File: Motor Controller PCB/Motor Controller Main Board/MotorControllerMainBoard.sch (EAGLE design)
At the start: 83 parts, among them T1 TEENSY_3.1_ALL_PINS

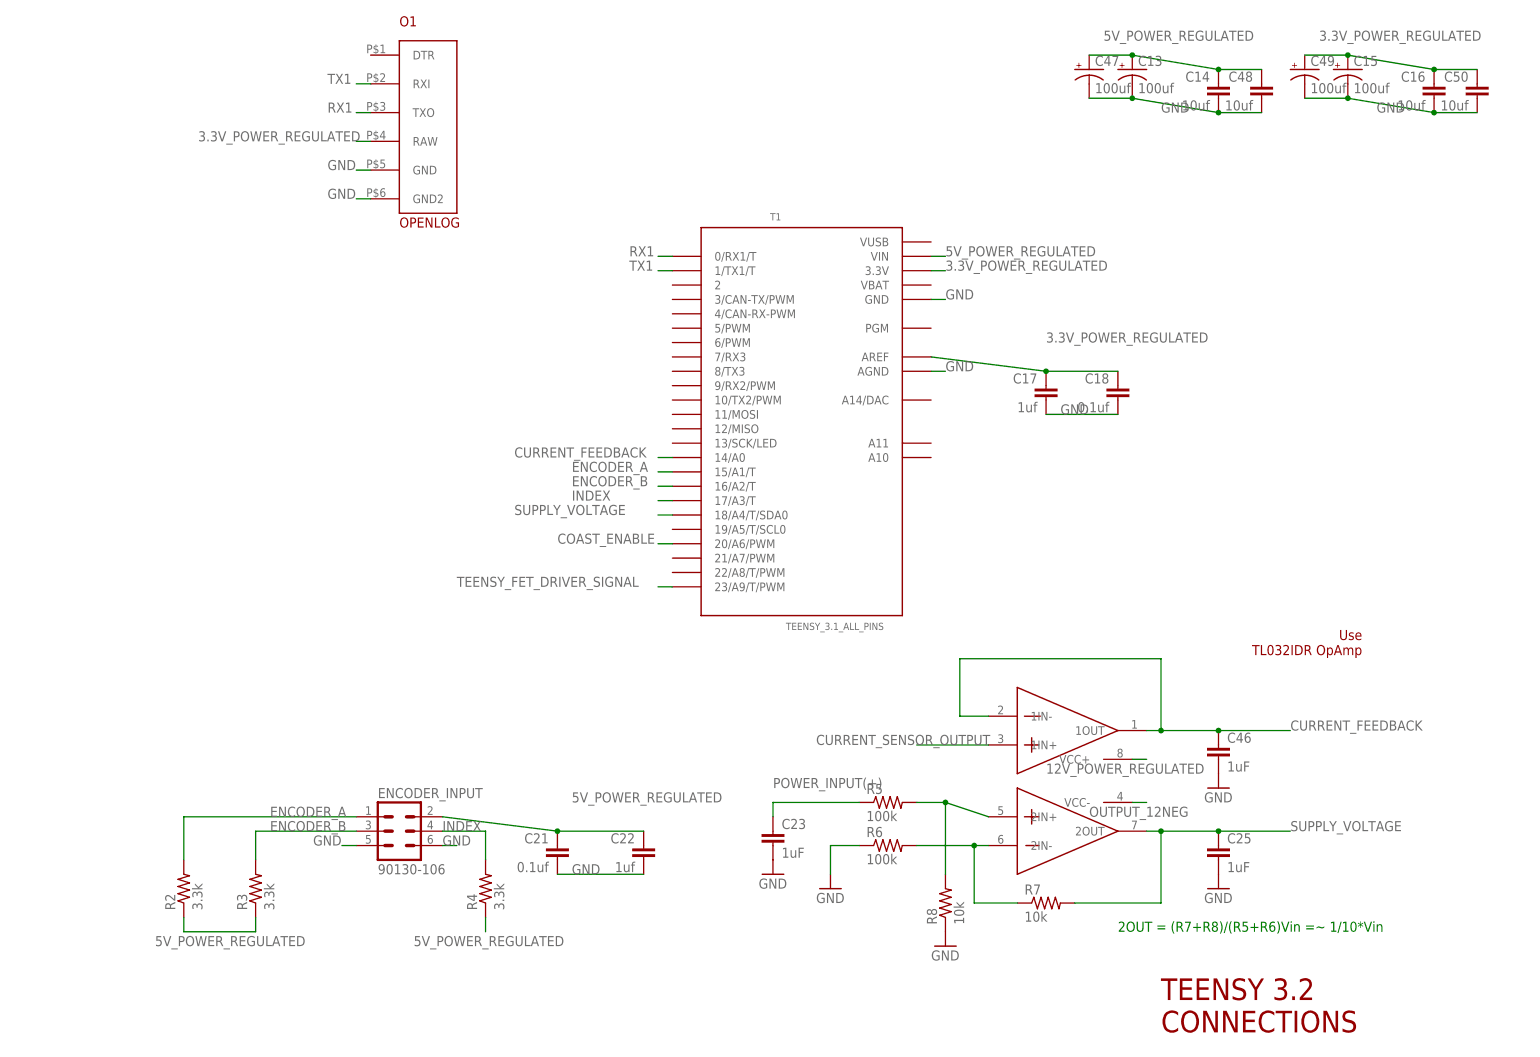
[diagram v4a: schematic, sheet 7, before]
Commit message: Routed majority of the power components
-Only thing left is stuff connected to teensy and other things i missed
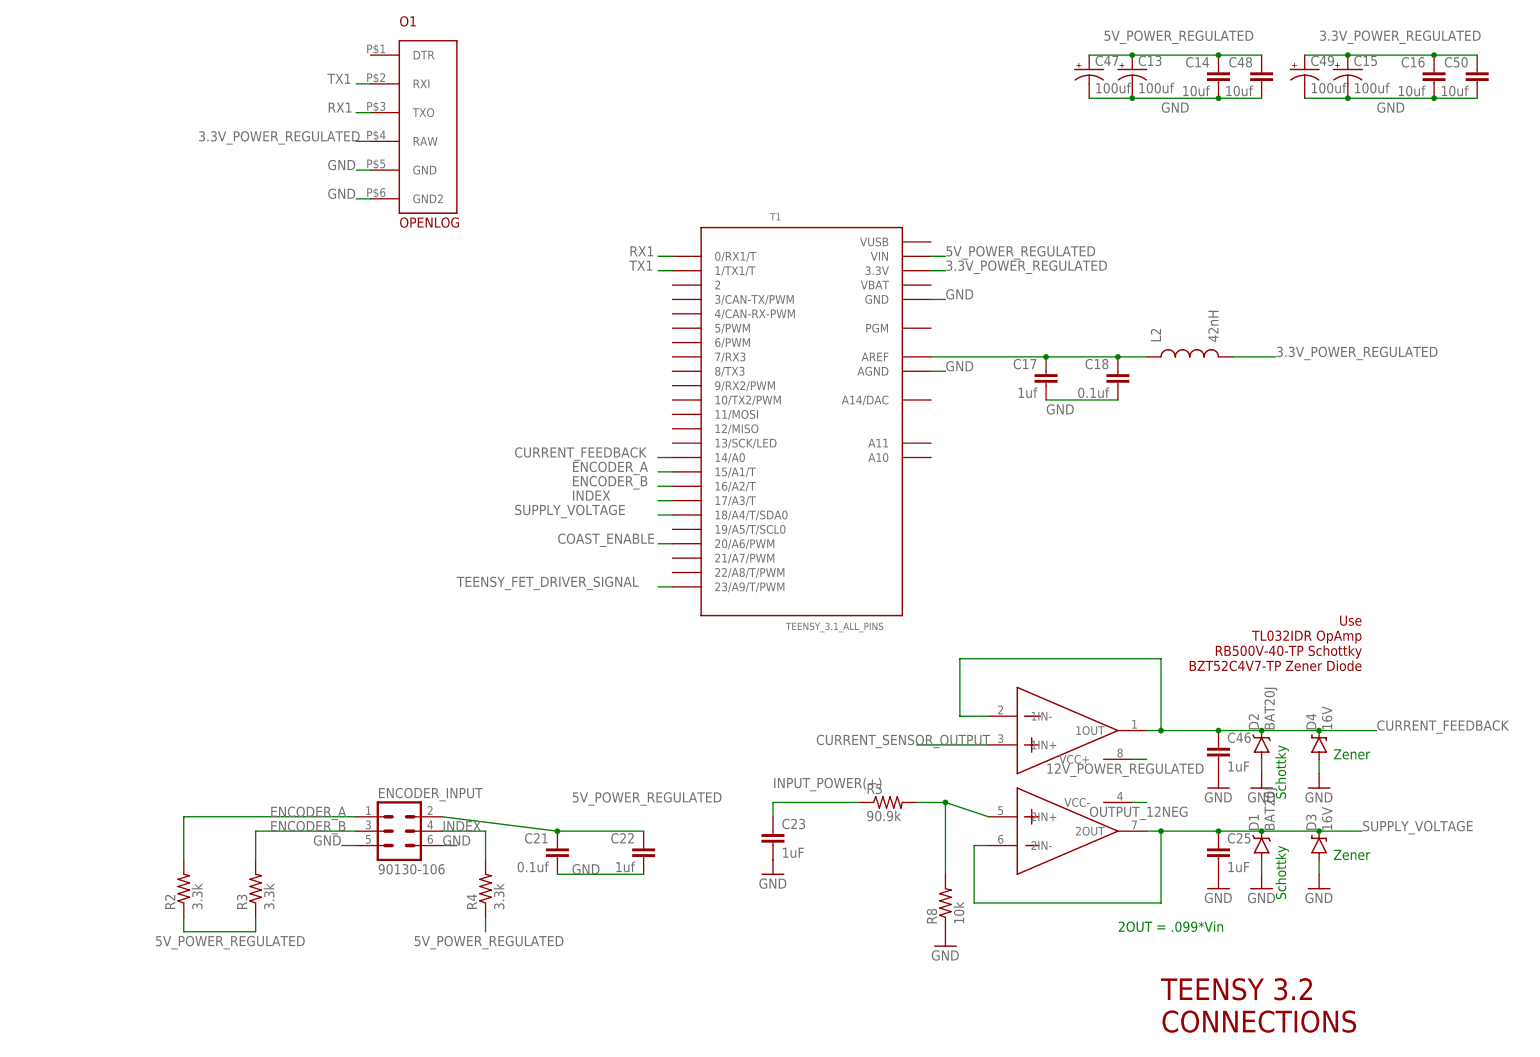
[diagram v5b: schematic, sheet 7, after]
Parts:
- removed R6: 100k, rcl:R-US_R0805
- removed R7: 10k, rcl:R-US_R0805
- added D1, D2: BAT20J, SparkFun-DiscreteSemi:DIODE-SCHOTTKY-BAT20J
- added D3, D4: 16V, SparkFun-DiscreteSemi:DIODE-ZENER16V
- added L2: 42nH, SparkFun (2015_10_14 22_27_04 UTC):INDUCTOR0805
- C55, C56, C57, C59, C60: value (none) -> 10uF
- R5: value 100k -> 90.9k
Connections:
- new net N$13: R9.11, SV2.2
- net 3.3V_POWER_REGULATED: now also L2.2; no longer C17.1, C18.1, T1.AREF
- net CURRENT_FEEDBACK: now also D2.C, D4.C
- net FET_DRIVER_SIGNAL: no longer R9.11, SV2.2
- net GND: now also D1.A, D2.A, D3.A, D4.A; no longer R6.1
- net INPUT_POWER(+): now also C23.1, R5.1
- net MOTOR_OUTPUT_(+): now also U$13.VIN, U$6.VIN
- net N$9: now also C17.1, C18.1, L2.1, T1.AREF; no longer AD8512ARZ.2IN-, R6.2, R7.1
- net POWER_INPUT(+): no longer C23.1, R5.1, U$13.VIN, U$6.VIN
- net SUPPLY_VOLTAGE: now also AD8512ARZ.2IN-, D1.C, D3.C; no longer R7.2
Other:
- note added: "2OUT = .099*Vin"
- note added: "Schottky"
- note added: "Use TL032IDR OpAmp RB500V-40-TP Schottky BZT52C4V7-TP Zener Diode"
- note added: "Zener"
- note removed: "2OUT = (R7+R8)/(R5+R6)Vin =~ 1/10*Vin"
- note removed: "Use TL032IDR OpAmp"
- moved on the sheet: C14, C16, C17, C18, C48, C50

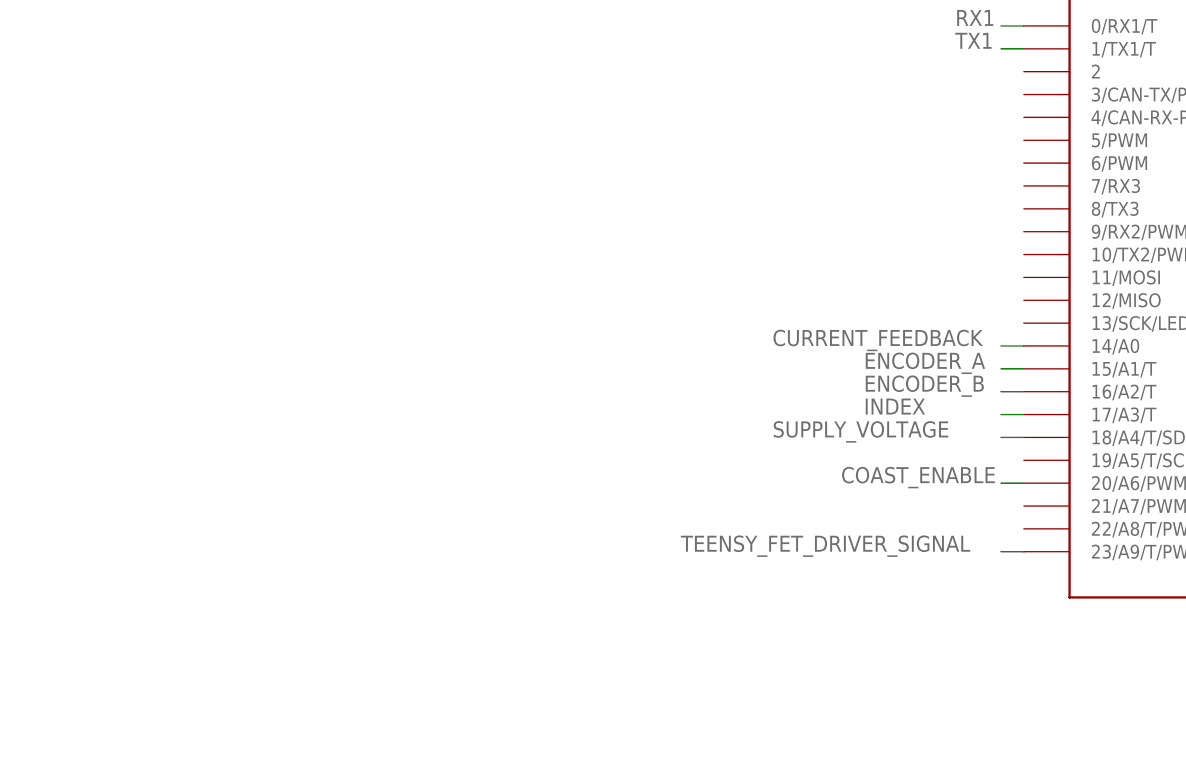
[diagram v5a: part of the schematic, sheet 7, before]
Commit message: Added Header, Worked on Digital Connections
Added 2x5 header for IO, added 1x3 header for Hall sensor. Worked on
some digital connections, still a work in progress.
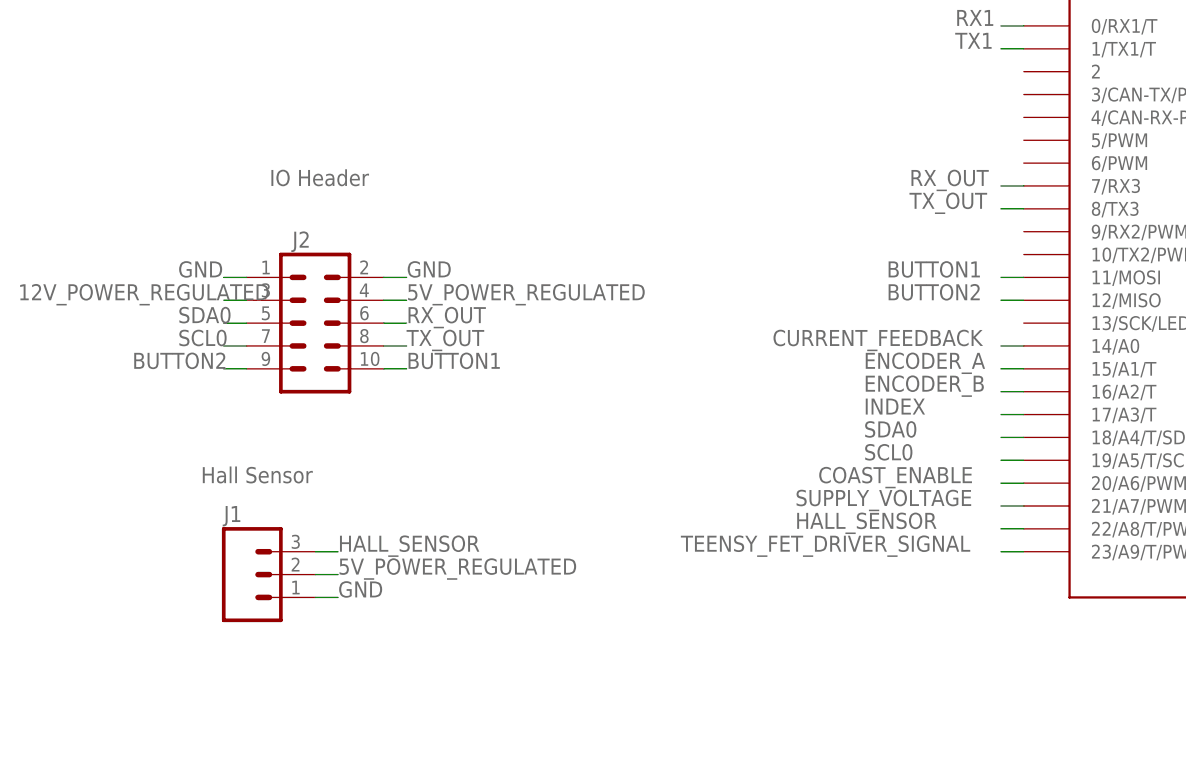
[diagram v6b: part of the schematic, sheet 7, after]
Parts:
- added J1: (no value), SparkFun-Connectors:M03PTH
- added J2: (no value), SparkFun-Connectors:M05X2NO_SILK
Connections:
- new net BUTTON1: J2.10, T1.11/MOSI
- new net BUTTON2: J2.9, T1.12/MISO
- new net HALL_SENSOR: J1.3, T1.22/A8/T/PWM
- new net RX_OUT: J2.6, T1.7/RX3
- new net SCL0: J2.7, T1.19/A5/T/SCL0
- new net SDA0: J2.5, T1.18/A4/T/SDA0
- new net TX_OUT: J2.8, T1.8/TX3
- net 12V_POWER_REGULATED: now also J2.3
- net 5V_POWER_REGULATED: now also J1.2, J2.4
- net GND: now also J1.1, J2.1, J2.2
- net SUPPLY_VOLTAGE: now also T1.21/A7/PWM; no longer T1.18/A4/T/SDA0
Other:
- note added: "Hall Sensor"
- note added: "IO Header"
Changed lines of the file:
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@@
 <part name="GND33" library="E-P-008-R1.2" deviceset="GND" device=""/>
 <part name="L2" library="SparkFun (2015_10_14 22_27_04 UTC)" deviceset="INDUCTOR" device="0805" value="42nH"/>
+<part name="J2" library="SparkFun-Connectors" deviceset="M05X2" device="NO_SILK"/>
+<part name="J1" library="SparkFun-Connectors" deviceset="M03" device="PTH"/>
 </parts>
 <sheets>
@@
 <text x="223.52" y="58.42" size="1.778" layer="91" rot="R270">Schottky</text>
 <text x="223.52" y="76.2" size="1.778" layer="91" rot="R270">Schottky</text>
+<text x="33.02" y="144.78" size="1.778" layer="95">IO Header</text>
+<text x="25.4" y="111.76" size="1.778" layer="95">Hall Sensor</text>
 </plain>
 <instances>
@@
 <instance part="GND33" gate="1" x="231.14" y="50.8"/>
 <instance part="L2" gate="G$1" x="208.28" y="144.78" rot="R90"/>
+<instance part="J2" gate="G$1" x="38.1" y="129.54"/>
+<instance part="J1" gate="J$1" x="30.48" y="101.6"/>
 </instances>
 <busses>
@@
 <wire x1="231.14" y1="55.88" x2="231.14" y2="53.34" width="0.1524" layer="91"/>
 </segment>
+<segment>
+<pinref part="J2" gate="G$1" pin="1"/>
+<wire x1="30.48" y1="134.62" x2="27.94" y2="134.62" width="0.1524" layer="91"/>
+<label x="22.86" y="134.62" size="1.778" layer="95"/>
+</segment>
+<segment>
+<pinref part="J2" gate="G$1" pin="2"/>
+<wire x1="45.72" y1="134.62" x2="48.26" y2="134.62" width="0.1524" layer="91"/>
+<label x="48.26" y="134.62" size="1.778" layer="95"/>
+</segment>
+<segment>
+<pinref part="J1" gate="J$1" pin="1"/>
+<wire x1="38.1" y1="99.06" x2="40.64" y2="99.06" width="0.1524" layer="91"/>
+<label x="40.64" y="99.06" size="1.778" layer="95"/>
+</segment>
 </net>
 <net name="5V_POWER_REGULATED" class="0">
@@
 <wire x1="83.82" y1="45.72" x2="83.82" y2="43.18" width="0.1524" layer="91"/>
 <label x="71.12" y="40.64" size="1.778" layer="95"/>
+</segment>
+<segment>
+<pinref part="J2" gate="G$1" pin="4"/>
+<wire x1="45.72" y1="132.08" x2="48.26" y2="132.08" width="0.1524" layer="91"/>
+<label x="48.26" y="132.08" size="1.778" layer="95"/>
+</segment>
+<segment>
+<pinref part="J1" gate="J$1" pin="2"/>
+<wire x1="38.1" y1="101.6" x2="40.64" y2="101.6" width="0.1524" layer="91"/>
+<label x="40.64" y="101.6" size="1.778" layer="95"/>
 </segment>
 </net>
@@
 <pinref part="T1" gate="G$1" pin="20/A6/PWM"/>
 <wire x1="116.84" y1="111.76" x2="114.3" y2="111.76" width="0.1524" layer="91"/>
-<label x="96.52" y="111.76" size="1.778" layer="95"/>
+<label x="93.98" y="111.76" size="1.778" layer="95"/>
 </segment>
 </net>
@@
 </segment>
 <segment>
-<pinref part="T1" gate="G$1" pin="18/A4/T/SDA0"/>
-<wire x1="116.84" y1="116.84" x2="114.3" y2="116.84" width="0.1524" layer="91"/>
-<label x="88.9" y="116.84" size="1.778" layer="95"/>
+<pinref part="T1" gate="G$1" pin="21/A7/PWM"/>
+<wire x1="116.84" y1="109.22" x2="114.3" y2="109.22" width="0.1524" layer="91"/>
+<label x="91.44" y="109.22" size="1.778" layer="95"/>
 </segment>
 </net>
@@
 <wire x1="198.12" y1="73.66" x2="200.66" y2="73.66" width="0.1524" layer="91"/>
 <label x="182.88" y="71.12" size="1.778" layer="95"/>
+</segment>
+<segment>
+<pinref part="J2" gate="G$1" pin="3"/>
+<wire x1="30.48" y1="132.08" x2="27.94" y2="132.08" width="0.1524" layer="91"/>
+<label x="5.08" y="132.08" size="1.778" layer="95"/>
 </segment>
 </net>
@@
 </segment>
 </net>
+<net name="BUTTON2" class="0">
+<segment>
+<pinref part="J2" gate="G$1" pin="9"/>
+<wire x1="30.48" y1="124.46" x2="27.94" y2="124.46" width="0.1524" layer="91"/>
+<label x="17.78" y="124.46" size="1.778" layer="95"/>
+</segment>
+<segment>
+<pinref part="T1" gate="G$1" pin="12/MISO"/>
+<wire x1="116.84" y1="132.08" x2="114.3" y2="132.08" width="0.1524" layer="91"/>
+<label x="101.6" y="132.08" size="1.778" layer="95"/>
+</segment>
+</net>
+<net name="BUTTON1" class="0">
+<segment>
+<pinref part="J2" gate="G$1" pin="10"/>
+<wire x1="45.72" y1="124.46" x2="48.26" y2="124.46" width="0.1524" layer="91"/>
+<label x="48.26" y="124.46" size="1.778" layer="95"/>
+</segment>
+<segment>
+<pinref part="T1" gate="G$1" pin="11/MOSI"/>
+<wire x1="116.84" y1="134.62" x2="114.3" y2="134.62" width="0.1524" layer="91"/>
+<label x="101.6" y="134.62" size="1.778" layer="95"/>
+</segment>
+</net>
+<net name="SDA0" class="0">
+<segment>
+<pinref part="T1" gate="G$1" pin="18/A4/T/SDA0"/>
+<wire x1="116.84" y1="116.84" x2="114.3" y2="116.84" width="0.1524" layer="91"/>
+<label x="99.06" y="116.84" size="1.778" layer="95"/>
+</segment>
+<segment>
+<pinref part="J2" gate="G$1" pin="5"/>
+<wire x1="30.48" y1="129.54" x2="27.94" y2="129.54" width="0.1524" layer="91"/>
+<label x="22.86" y="129.54" size="1.778" layer="95"/>
+</segment>
+</net>
+<net name="SCL0" class="0">
+<segment>
+<pinref part="T1" gate="G$1" pin="19/A5/T/SCL0"/>
+<wire x1="116.84" y1="114.3" x2="114.3" y2="114.3" width="0.1524" layer="91"/>
+<label x="99.06" y="114.3" size="1.778" layer="95"/>
+</segment>
+<segment>
+<pinref part="J2" gate="G$1" pin="7"/>
+<wire x1="30.48" y1="127" x2="27.94" y2="127" width="0.1524" layer="91"/>
+<label x="22.86" y="127" size="1.778" layer="95"/>
+</segment>
+</net>
+<net name="RX_OUT" class="0">
+<segment>
+<pinref part="T1" gate="G$1" pin="7/RX3"/>
+<wire x1="116.84" y1="144.78" x2="114.3" y2="144.78" width="0.1524" layer="91"/>
+<label x="104.14" y="144.78" size="1.778" layer="95"/>
+</segment>
+<segment>
+<pinref part="J2" gate="G$1" pin="6"/>
+<wire x1="45.72" y1="129.54" x2="48.26" y2="129.54" width="0.1524" layer="91"/>
+<label x="48.26" y="129.54" size="1.778" layer="95"/>
+</segment>
+</net>
+<net name="TX_OUT" class="0">
+<segment>
+<pinref part="T1" gate="G$1" pin="8/TX3"/>
+<wire x1="116.84" y1="142.24" x2="114.3" y2="142.24" width="0.1524" layer="91"/>
+<label x="104.14" y="142.24" size="1.778" layer="95"/>
+</segment>
+<segment>
+<pinref part="J2" gate="G$1" pin="8"/>
+<wire x1="45.72" y1="127" x2="48.26" y2="127" width="0.1524" layer="91"/>
+<label x="48.26" y="127" size="1.778" layer="95"/>
+</segment>
+</net>
+<net name="HALL_SENSOR" class="0">
+<segment>
+<pinref part="T1" gate="G$1" pin="22/A8/T/PWM"/>
+<wire x1="116.84" y1="106.68" x2="114.3" y2="106.68" width="0.1524" layer="91"/>
+<label x="91.44" y="106.68" size="1.778" layer="95"/>
+</segment>
+<segment>
+<pinref part="J1" gate="J$1" pin="3"/>
+<wire x1="38.1" y1="104.14" x2="40.64" y2="104.14" width="0.1524" layer="91"/>
+<label x="40.64" y="104.14" size="1.778" layer="95"/>
+</segment>
+</net>
